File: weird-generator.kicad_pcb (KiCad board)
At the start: 2 copper layers, 66 parts, among them J1 Battery Connector, J2 Audio Out, Q1 2N3904, Q2 2N3904, SW1 Unusual, SW2 Unusual, SW3 Wacky, SW4 Wacky, SW5 Wacky Out, SW6 Wacky Out, SW7 ON/OFF, U1 40106, U3 LM741

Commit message: Initial PCB iteration
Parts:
- RV1, RV10, RV11, RV2, RV3, RV4, RV5, RV6, RV7, RV8, RV9: footprint Potentiometer_THT:Potentiometer_Omeg_PC16BU_Vertical -> fx_synth_parts:potentiometer_fx_connector
- moved SW7 172.4 mm to (95.3, 76.6)
- moved R2 155.6 mm to (89.5, 57.1), turned to -90 degrees
- moved R4 150.9 mm to (97.3, 57.1), turned to -90 degrees
- moved R1 144.9 mm to (89.6, 101.6), turned to 90 degrees
- moved R3 137.7 mm to (97.4, 101.6), turned to 90 degrees
- moved R7 137.6 mm to (117.5, 57.1), turned to -90 degrees
- moved D2 136.7 mm to (140.0, 57.1), turned to -90 degrees
- moved R8 132.7 mm to (120.5, 64.8), turned to 90 degrees
- moved D1 130.7 mm to (140.1, 101.6), turned to 90 degrees
- moved SW2 124.7 mm to (124.2, 58.4)
- moved SW4 122.1 mm to (136.2, 58.4)
- moved R5 118.6 mm to (117.7, 101.6), turned to 90 degrees
- moved R6 118.3 mm to (120.6, 94.0), turned to -90 degrees
- moved SW1 114.7 mm to (124.2, 100.4), turned to 180 degrees
- moved R11 114.0 mm to (148.0, 57.1), turned to -90 degrees
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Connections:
- C1 pad 2: unconnected-(C1-Pad2) -> -BATT
- C10 pad 1: Net-(C10-Pad1) -> +BATT
- C10 pad 2: Net-(C10-Pad2) -> -BATT
- C11 pad 1: Net-(SW7-B) -> +BATT
- C11 pad 2: Net-(J1-Pin_1) -> -BATT
- C13 pad 2: unconnected-(C13-Pad2) -> -BATT
- C2 pad 2: unconnected-(C2-Pad2) -> -BATT
- C3 pad 2: unconnected-(C3-Pad2) -> -BATT
- C4 pad 2: unconnected-(C4-Pad2) -> -BATT
- C7 pad 2: unconnected-(C7-Pad2) -> -BATT
- C8 pad 2: unconnected-(C8-Pad2) -> -BATT
- C9 pad 1: Net-(C10-Pad1) -> +BATT
- C9 pad 2: Net-(C10-Pad2) -> -BATT
- J1 pad 1: Net-(J1-Pin_1) -> -BATT
- J2 pad 2: unconnected-(J2-Pin_2-Pad2) -> -BATT
- R17 pad 2: unconnected-(R17-Pad2) -> -BATT
- R20 pad 2: unconnected-(R20-Pad2) -> -BATT
- RV5 pad 3: unconnected-(RV5-Pad3) -> -BATT
- RV6 pad 3: unconnected-(RV6-Pad3) -> -BATT
- SW1 pad 2: unconnected-(SW1-B-Pad2) -> -BATT
- SW2 pad 2: unconnected-(SW2-B-Pad2) -> -BATT
- SW7 pad 2: Net-(SW7-B) -> +BATT
- U1 pad 14: unconnected-(U1G-VDD-Pad14) -> +BATT
- U1 pad 7: unconnected-(U1G-VSS-Pad7) -> -BATT
- U3 pad 4: unconnected-(U3-V--Pad4) -> -BATT
- U3 pad 7: unconnected-(U3-V+-Pad7) -> +BATT
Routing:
- net Net-(Q2-B): track 0.00 -> 40.8 mm
- net Net-(Q1-B): track 0.00 -> 39.3 mm
- net Net-(RV3-Pad1): track 0.00 -> 23.2 mm
- net Net-(RV4-Pad1): track 0.00 -> 23.1 mm
- net Net-(C15-Pad1): track 0.00 -> 14.8 mm
- net Net-(C6-Pad1): track 0.00 -> 14.3 mm
- net Net-(C5-Pad1): track 0.00 -> 14.3 mm
- net Net-(C3-Pad1): track 0.00 -> 12.9 mm
- net Net-(C4-Pad1): track 0.00 -> 12.5 mm
- net /filter in: track 0.00 -> 9.70 mm
- net Net-(U3--): track 0.00 -> 8.97 mm
- net Net-(R12-Pad2): track 0.00 -> 8.83 mm
- net Net-(R10-Pad2): track 0.00 -> 8.83 mm
- net Net-(D2-A): track 0.00 -> 8.81 mm
- net Net-(Q1-C): track 0.00 -> 8.05 mm
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- added copper zone on B.Cu, net -BATT
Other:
- board outline added: 120 x 54 mm

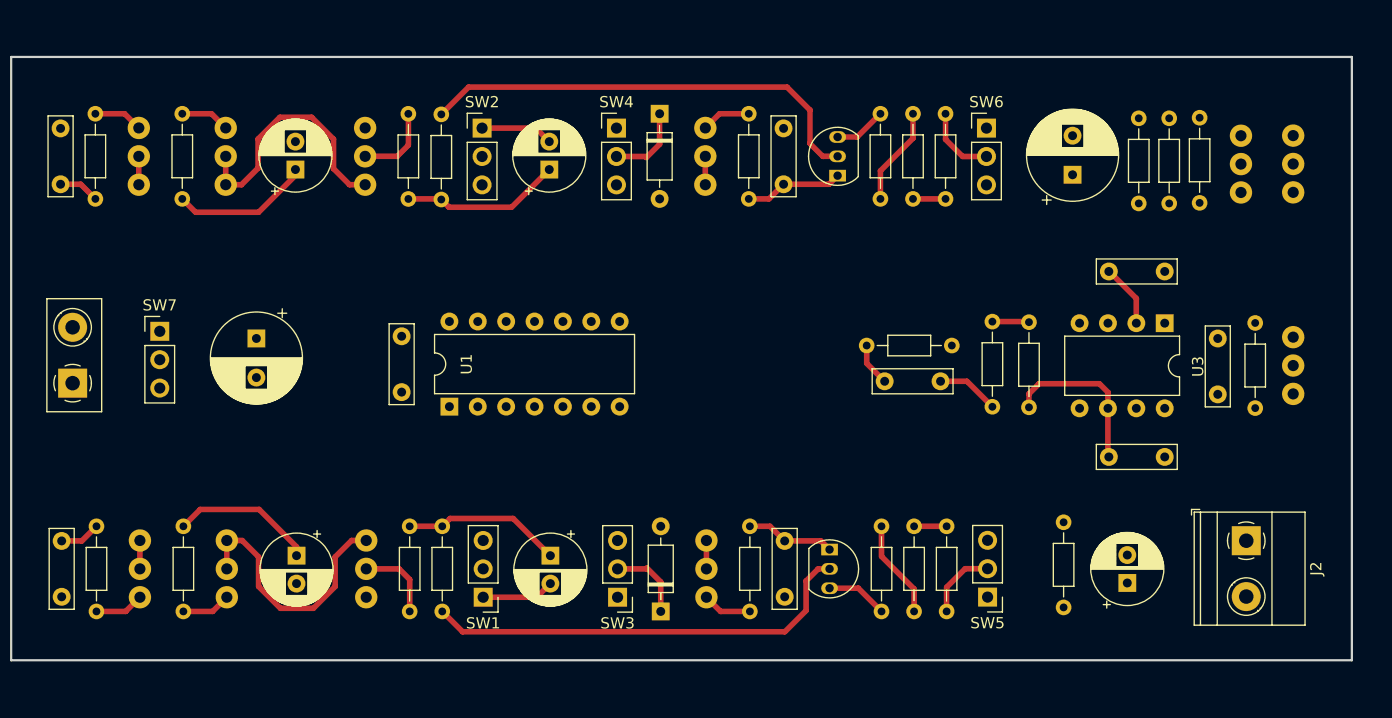
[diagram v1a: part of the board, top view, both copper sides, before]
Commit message: Completed trace routing
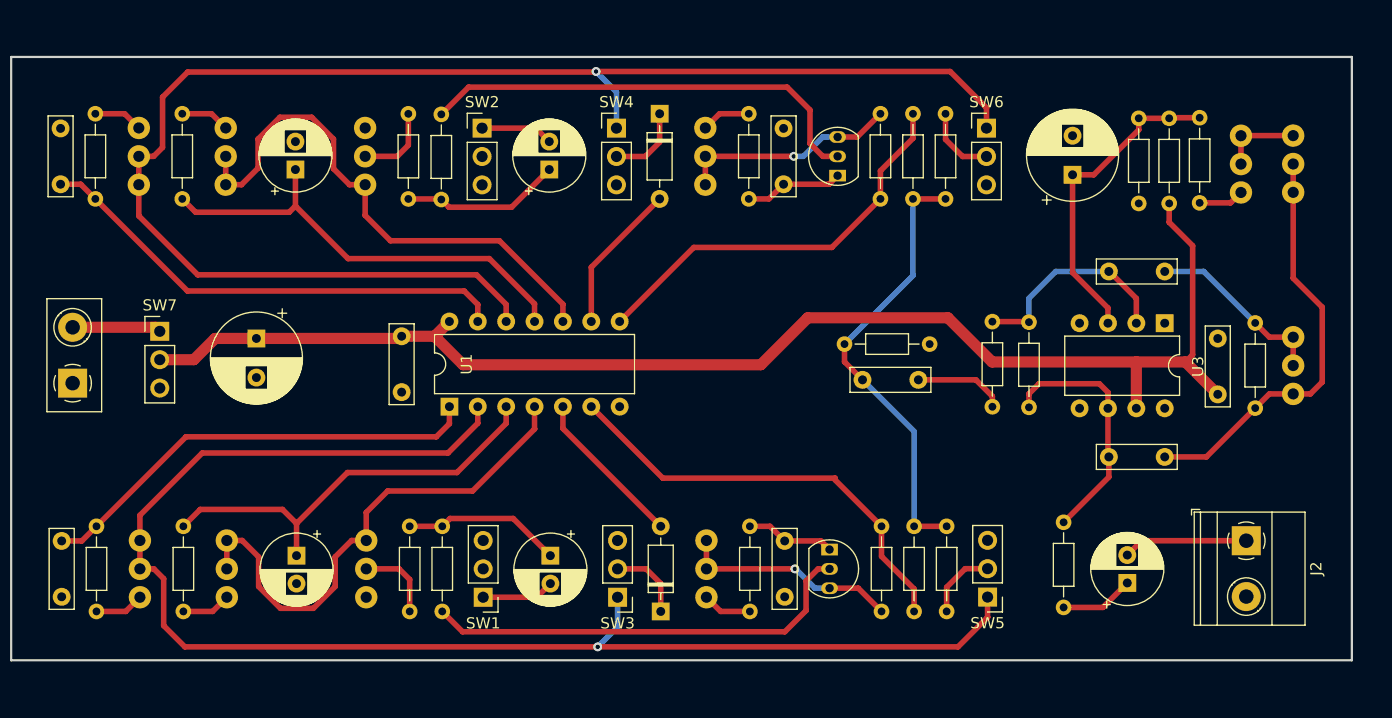
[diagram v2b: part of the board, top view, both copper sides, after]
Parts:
- moved C12 1.99 mm to (158.2, 80.9)
- moved R17 1.99 mm to (156.6, 77.7)
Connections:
- R19 pad 1: unconnected-(R19-Pad1) -> +BATT
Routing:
- net Net-(SW4-A): track 2.54 -> 133.7 mm, vias 0 -> 1
- net Net-(SW3-A): track 2.54 -> 129.2 mm, vias 0 -> 1
- net +BATT: track 0.00 -> 122.6 mm
- net Net-(C2-Pad1): track 3.66 -> 43.3 mm
- net Net-(C15-Pad2): track 0.00 -> 37.5 mm
- net Net-(C1-Pad1): track 3.66 -> 40.6 mm
- net /filter in: track 9.70 -> 40.3 mm
- net Net-(R10-Pad2): track 8.83 -> 39.3 mm
- net Net-(U3-+): track 0.00 -> 28.7 mm
- net Net-(C4-Pad1): track 12.5 -> 40.7 mm
- net Net-(R12-Pad2): track 8.83 -> 36.7 mm
- net Net-(RV4-Pad1): track 23.1 -> 48.4 mm
- net Net-(C3-Pad1): track 12.9 -> 38.1 mm
- net Net-(RV3-Pad1): track 23.2 -> 45.8 mm
- net Net-(C14-Pad2): track 0.00 -> 16.5 mm
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
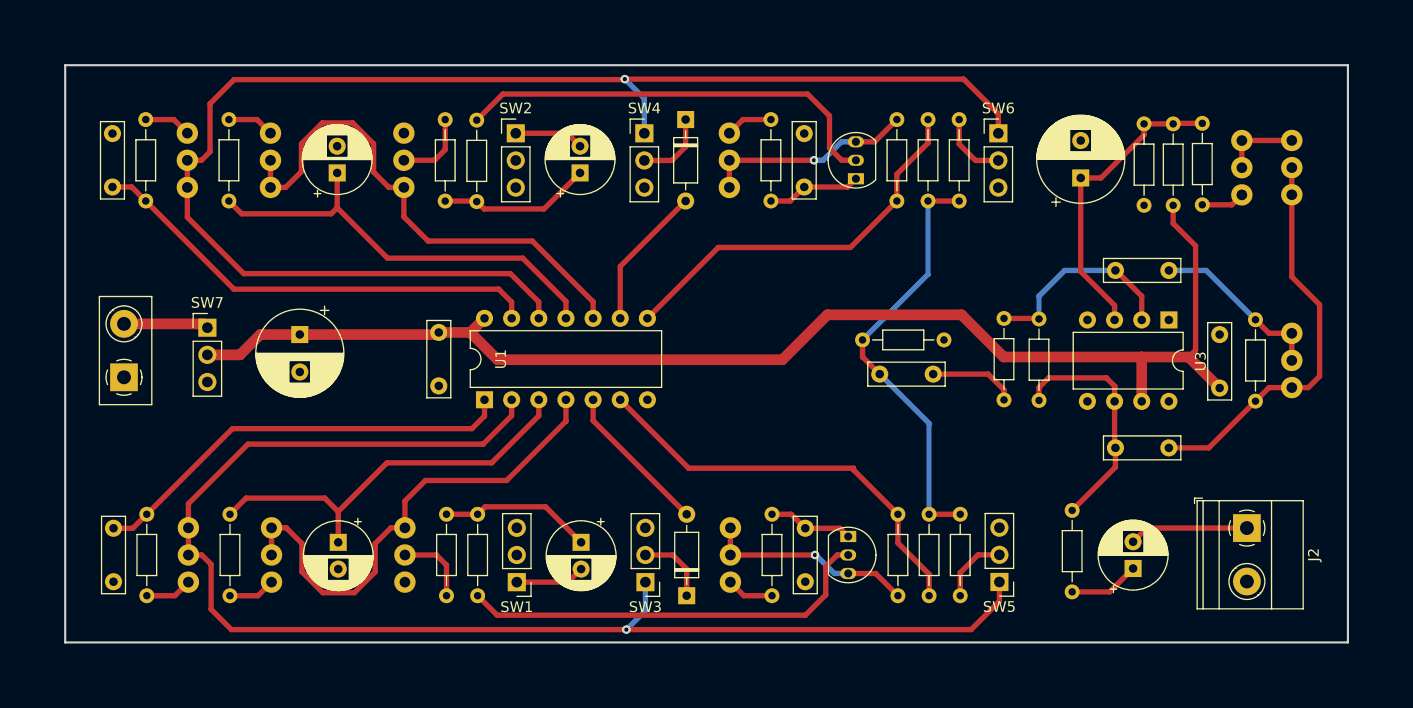
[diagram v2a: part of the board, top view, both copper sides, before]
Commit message: Rearranged components and shrunk board
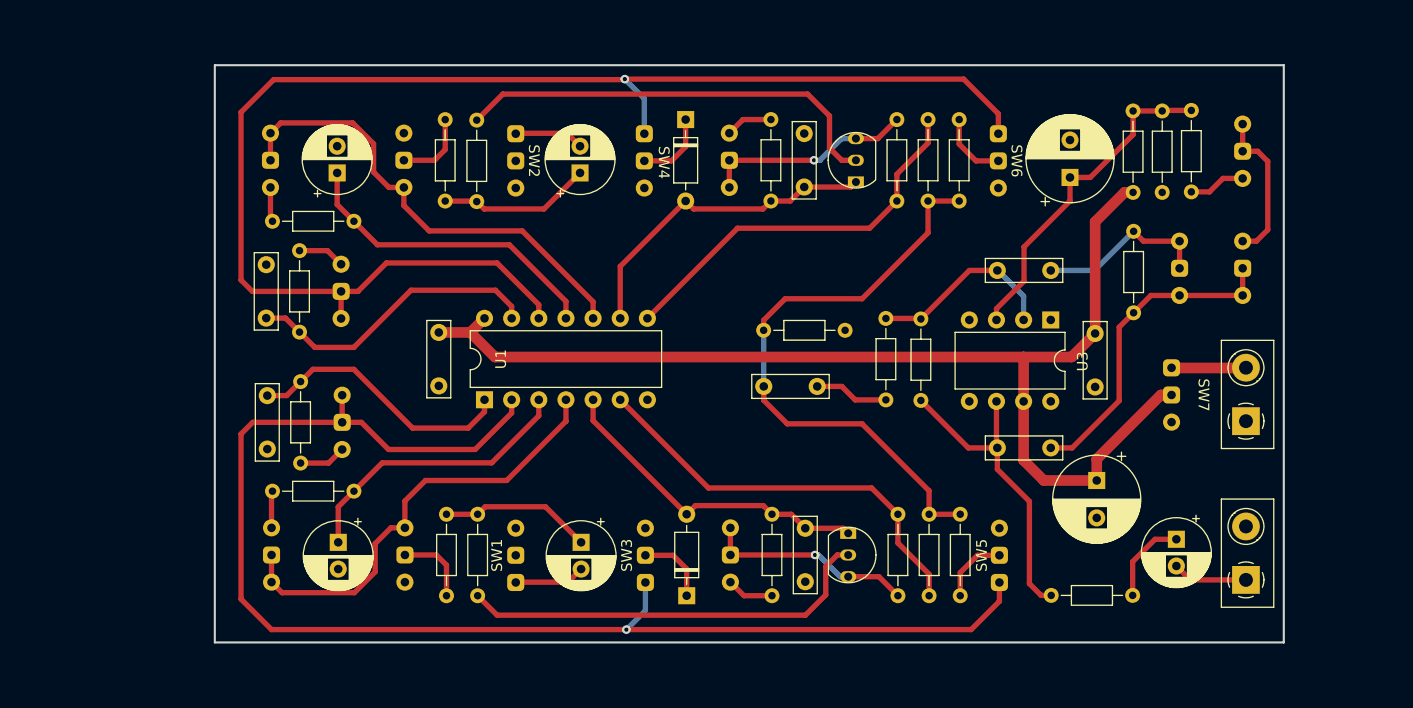
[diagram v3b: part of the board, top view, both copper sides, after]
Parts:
- SW1, SW2, SW3, SW4, SW5, SW6, SW7: footprint Connector_PinHeader_2.54mm:PinHeader_1x03_P2.54mm_Vertical -> fx_synth_parts:switch_fx_connector
- moved J1 105.0 mm to (192.5, 85.3)
- moved SW7 90.4 mm to (185.5, 82.8), turned to -90 degrees
- moved C11 75.8 mm to (178.5, 90.8)
- moved C1 19.0 mm to (100.9, 82.9)
- moved R1 19.0 mm to (104.0, 89.2)
- moved RV1 19.0 mm to (107.9, 85.4)
- moved C2 18.9 mm to (100.8, 75.7)
- moved R2 18.9 mm to (103.9, 69.3)
- moved RV2 18.9 mm to (107.8, 73.2)
- moved R23 14.1 mm to (181.9, 67.5)
- moved RV11 13.6 mm to (186.2, 71.0)
- moved C9 12.7 mm to (178.3, 77.1), turned to -90 degrees
- moved C14 11.1 mm to (169.2, 71.2)
- moved C15 11.1 mm to (169.2, 87.8)
- moved U3 11.1 mm to (174.2, 75.8)
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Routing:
- net /filter in: track 40.3 -> 56.2 mm
- net Net-(C2-Pad1): track 43.3 -> 28.1 mm
- net Net-(C1-Pad1): track 40.6 -> 25.4 mm
- net +BATT: track 122.6 -> 109.3 mm
- net Net-(C4-Pad1): track 40.7 -> 29.7 mm
- net Net-(C3-Pad1): track 38.1 -> 27.1 mm
- net Net-(D1-A): track 22.3 -> 30.9 mm
- net Net-(D2-A): track 22.3 -> 30.8 mm
- net Net-(C15-Pad1): track 22.3 -> 29.8 mm
- net Net-(RV10-Pad3): track 7.22 -> 14.5 mm
- net Net-(C15-Pad2): track 37.5 -> 30.4 mm
- net Net-(RV4-Pad1): track 48.4 -> 44.1 mm
- net Net-(J2-Pin_1): track 11.2 -> 7.05 mm
- net Net-(RV3-Pad1): track 45.8 -> 42.2 mm
- net Net-(U3-+): track 28.7 -> 31.4 mm
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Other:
- board size 120 x 54 mm -> 100 x 54 mm

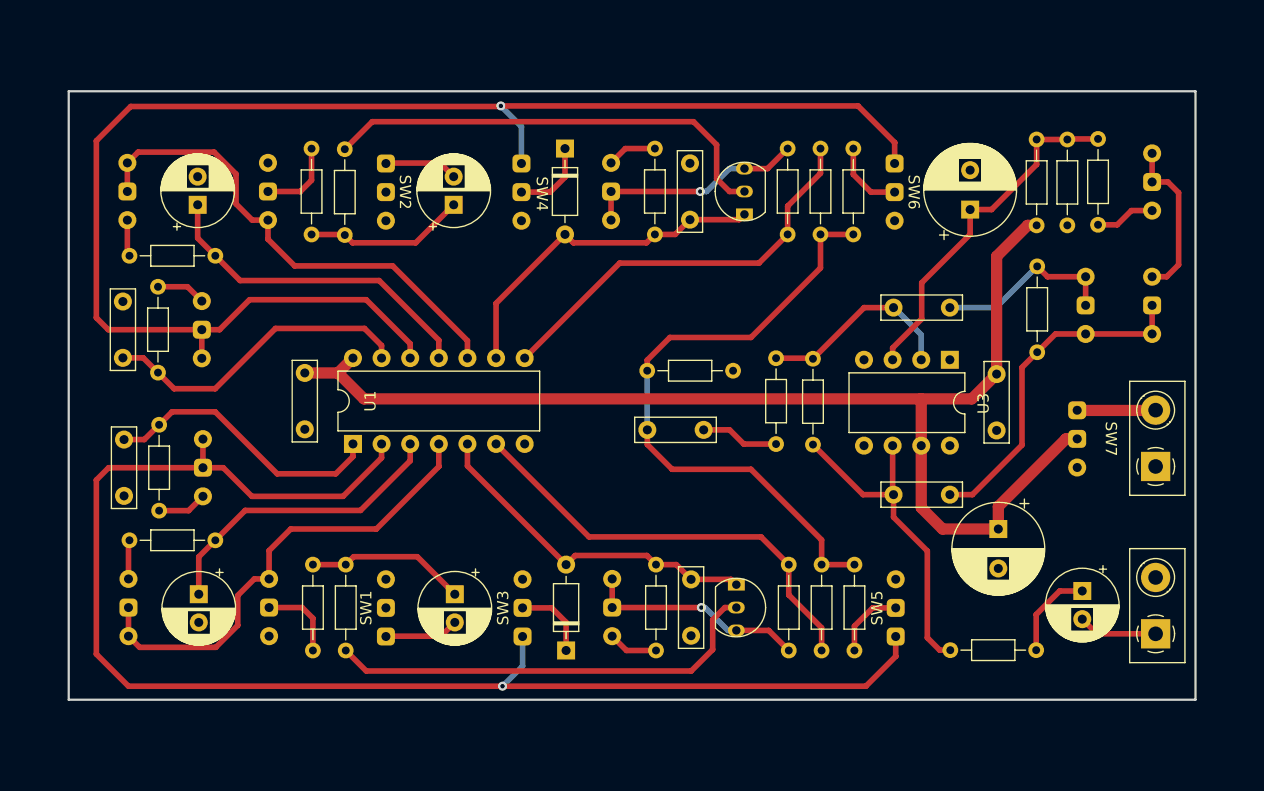
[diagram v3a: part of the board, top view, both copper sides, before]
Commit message: Added mounting holes
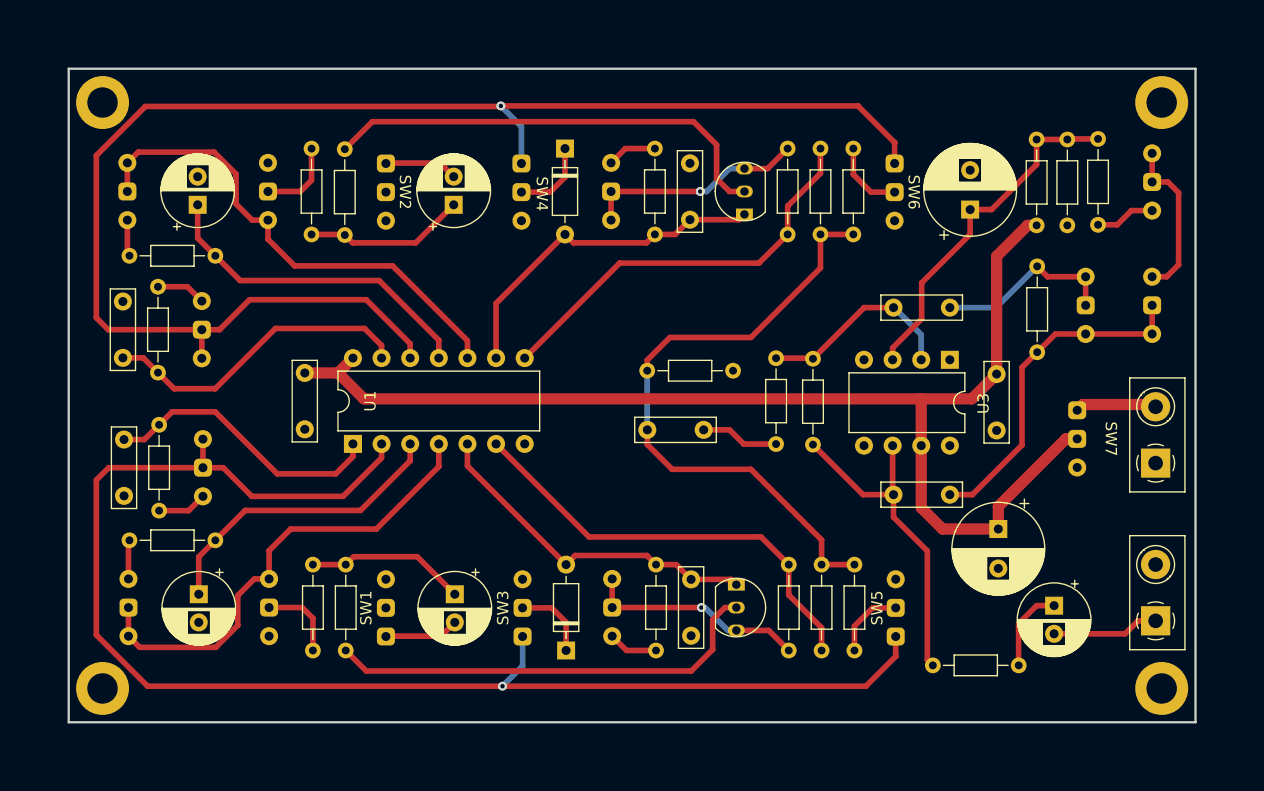
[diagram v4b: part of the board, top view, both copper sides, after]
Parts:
- added REF**: MountingHole_2.7mm_M2.5_DIN965_Pad, MountingHole:MountingHole_2.7mm_M2.5_DIN965_Pad, F.Cu at (99.0, 105.0)
- added REF**: MountingHole_2.7mm_M2.5_DIN965_Pad, MountingHole:MountingHole_2.7mm_M2.5_DIN965_Pad, F.Cu at (193.0, 105.0)
- added REF**: MountingHole_2.7mm_M2.5_DIN965_Pad, MountingHole:MountingHole_2.7mm_M2.5_DIN965_Pad, F.Cu at (99.0, 53.0)
- added REF**: MountingHole_2.7mm_M2.5_DIN965_Pad, MountingHole:MountingHole_2.7mm_M2.5_DIN965_Pad, F.Cu at (193.0, 53.0)
- moved C16 2.82 mm to (183.4, 97.7)
- moved R24 2.06 mm to (172.7, 103.0)
- moved J2 1.15 mm to (192.5, 99.0)
- moved J1 0.30 mm to (192.5, 85.0)
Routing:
- net Net-(J2-Pin_1): track 7.05 -> 9.49 mm
- net Net-(SW3-A): track 127.6 -> 126.6 mm
- net Net-(SW4-A): track 131.8 -> 131.0 mm
- net Net-(C16-Pad1): track 8.12 -> 7.52 mm
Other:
- board size 100 x 54 mm -> 100 x 58 mm
